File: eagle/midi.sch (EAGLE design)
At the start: 63 parts, among them CON1 EXPANSION-PORT, IC1 74LS14, IC10 EMI-FILTER, IC11 EMI-FILTER, IC2 SST39VF1681, IC3 6N138SMD, IC4 48MHz, IC5 CY61228EV30, IC6 XC95144XL_TQ100, IC8 MCP1703DB, IC9 74LVC8T245

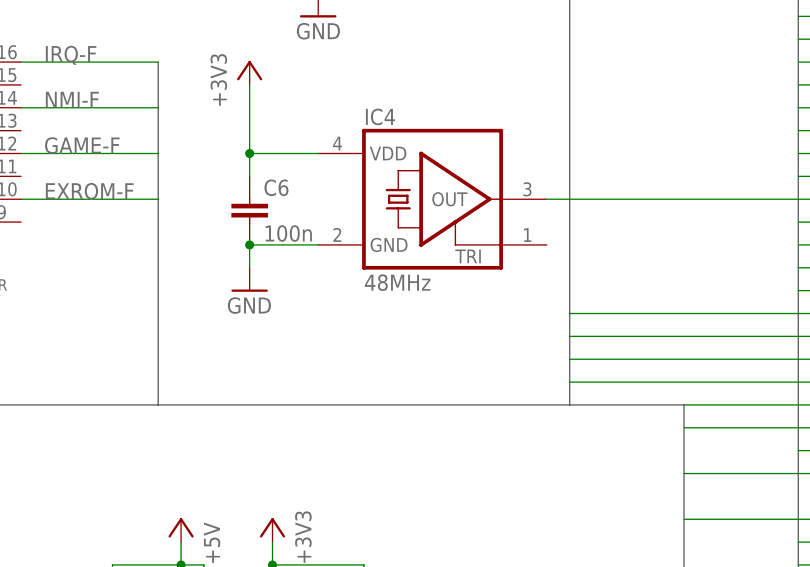
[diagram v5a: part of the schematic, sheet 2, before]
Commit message: new datasheets, EasyFlash starter test and cleanups
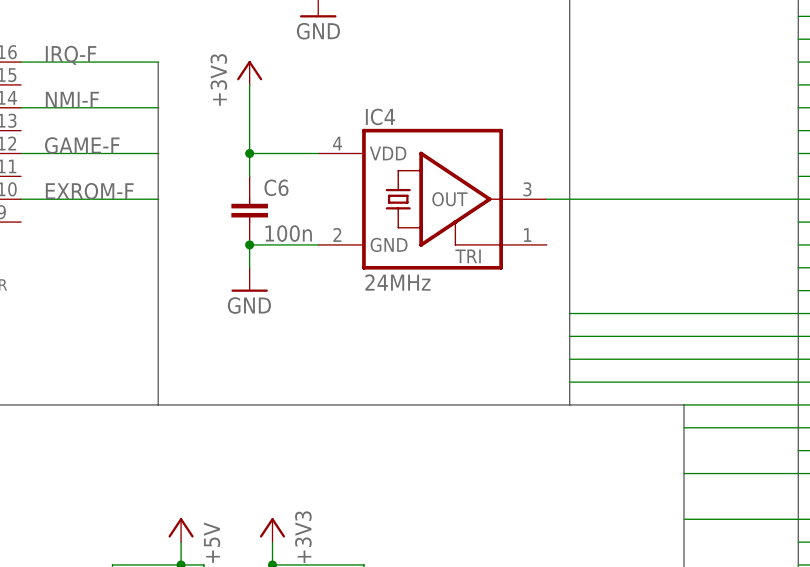
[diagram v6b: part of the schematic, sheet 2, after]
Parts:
- IC4: value 48MHz -> 24MHz
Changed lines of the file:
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@@
 <part name="R9" library="rcl" deviceset="R-EU_" device="R1206" value="220"/>
 <part name="IC3" library="6n138" deviceset="6N138" device="SMD"/>
-<part name="IC4" library="cartridge" deviceset="ASE" device="" value="48MHz"/>
+<part name="IC4" library="cartridge" deviceset="ASE" device="" value="24MHz"/>
 <part name="P+2" library="supply1" deviceset="+5V" device=""/>
 <part name="C9" library="rcl" deviceset="C-EU" device="C0603" value="100n"/>

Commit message: schematic cleanup and added to documentation
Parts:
- R19, R8: value 10k -> 10k, not populated
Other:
- note added: "CPLD, RAM and flash"
- note added: "MIDI and expansion port"
- note added: "Power Supply"
- moved on the sheet: 3V3, C1, C10, C11, C12, C13, C14, C15, C16, C2, C3, C4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
